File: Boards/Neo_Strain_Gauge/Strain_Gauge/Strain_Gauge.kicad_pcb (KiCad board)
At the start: 2 copper layers, 85 x 56 mm, 71 parts, among them J1 Screw_Terminal_01x03, J2 Screw_Terminal_01x03, J3 Screw_Terminal_01x03, J4 Screw_Terminal_01x03, J5 Conn_01x02, J6 USB_B_Micro, J7 Conn_02x10_Counter_Clockwise, J8 Conn_02x12_Counter_Clockwise, U1 W25Q128JVS, U2 NCP1117-3.3_SOT223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

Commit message: Hopefully final revision
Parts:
- moved TP1 0.39 mm to (147.4, 76.0)
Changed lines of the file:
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@@
   )
   (footprint "TestPoint:TestPoint_THTPad_D1.0mm_Drill0.5mm" (layer "F.Cu")
-    (at 147.61 76.36)
+    (at 147.4 76.03)
     (descr "THT pad as test Point, diameter 1.0mm, hole diameter 0.5mm")
     (tags "test point THT pad")
@@
   (segment (start 155.03103 70.64897) (end 163.51897 70.64897) (width 0.127) (layer "B.Cu") (net 77))
   (segment (start 155.08 72.27) (end 155.08 71.866886) (width 0.127) (layer "F.Cu") (net 80))
-  (segment (start 147.61 77.48) (end 147.61 76.36) (width 0.127) (layer "F.Cu") (net 80))
-  (segment (start 146.1535 78.9365) (end 147.61 77.48) (width 0.127) (layer "F.Cu") (net 80))
+  (segment (start 147.61 77.48) (end 146.1535 78.9365) (width 0.127) (layer "F.Cu") (net 80))
   (segment (start 157.06 71.2) (end 157.5625 71.2) (width 0.127) (layer "F.Cu") (net 80))
   (segment (start 151.62 73.47) (end 146.1535 78.9365) (width 0.127) (layer "F.Cu") (net 80))
   (segment (start 155.08 71.866886) (end 155.868488 71.078398) (width 0.127) (layer "F.Cu") (net 80))
   (segment (start 146.1535 78.9365) (end 134.577466 78.9365) (width 0.127) (layer "F.Cu") (net 80))
+  (segment (start 147.4 76.03) (end 147.61 76.24) (width 0.127) (layer "F.Cu") (net 80))
   (segment (start 156.938398 71.078398) (end 157.06 71.2) (width 0.127) (layer "F.Cu") (net 80))
   (segment (start 155.868488 71.078398) (end 156.938398 71.078398) (width 0.127) (layer "F.Cu") (net 80))
   (segment (start 134.577466 78.9365) (end 133.35 80.163966) (width 0.127) (layer "F.Cu") (net 80))
+  (segment (start 147.61 76.24) (end 147.61 77.48) (width 0.127) (layer "F.Cu") (net 80))
   (segment (start 133.35 80.163966) (end 133.35 80.5625) (width 0.127) (layer "F.Cu") (net 80))
   (via (at 155.08 72.27) (size 0.6) (drill 0.3) (layers "F.Cu" "B.Cu") (net 80))
@@
   (segment (start 151.62 73.47) (end 152.92 72.17) (width 0.127) (layer "B.Cu") (net 80))
   (segment (start 137.27 84.86) (end 136.16 83.75) (width 0.127) (layer "F.Cu") (net 81))
+  (segment (start 142.650412 85.514412) (end 145.795588 85.514412) (width 0.127) (layer "F.Cu") (net 81))
   (segment (start 136.16 83.75) (end 135.0375 83.75) (width 0.127) (layer "F.Cu") (net 81))
-  (segment (start 144.334824 83.83) (end 147.49 83.83) (width 0.127) (layer "F.Cu") (net 81))
   (segment (start 156.101898 71.641898) (end 156.143796 71.6) (width 0.127) (layer "F.Cu") (net 81))
-  (segment (start 142.650412 85.514412) (end 144.334824 83.83) (width 0.127) (layer "F.Cu") (net 81))
+  (segment (start 147.48 83.83) (end 147.49 83.83) (width 0.127) (layer "F.Cu") (net 81))
+  (segment (start 145.795588 85.514412) (end 147.48 83.83) (width 0.127) (layer "F.Cu") (net 81))
   (segment (start 156.143796 71.6) (end 157.5625 71.6) (width 0.127) (layer "F.Cu") (net 81))
   (via (at 142.650412 85.514412) (size 0.8) (drill 0.4) (layers "F.Cu" "B.Cu") (net 81))
   (via (at 156.101898 71.641898) (size 0.6) (drill 0.3) (layers "F.Cu" "B.Cu") (net 81))
   (via (at 137.27 84.86) (size 0.6) (drill 0.3) (layers "F.Cu" "B.Cu") (net 81))
-  (segment (start 143.39 85.09) (end 142.965588 85.514412) (width 0.127) (layer "B.Cu") (net 81))
+  (segment (start 143.39 85.09) (end 143.074824 85.09) (width 0.127) (layer "B.Cu") (net 81))
   (segment (start 152.740789 73.611659) (end 150.755948 75.5965) (width 0.127) (layer "B.Cu") (net 81))
   (segment (start 156.101898 71.641898) (end 155.8265 71.917296) (width 0.127) (layer "B.Cu") (net 81))
+  (segment (start 143.074824 85.09) (end 142.650412 85.514412) (width 0.127) (layer "B.Cu") (net 81))
   (segment (start 155.8265 71.917296) (end 155.8265 73.282069) (width 0.127) (layer "B.Cu") (net 81))
   (segment (start 155.49691 73.611659) (end 152.740789 73.611659) (width 0.127) (layer "B.Cu") (net 81))
   (segment (start 145.293 83.187) (end 143.39 85.09) (width 0.127) (layer "B.Cu") (net 81))
   (segment (start 155.8265 73.282069) (end 155.49691 73.611659) (width 0.127) (layer "B.Cu") (net 81))
-  (segment (start 142.965588 85.514412) (end 142.650412 85.514412) (width 0.127) (layer "B.Cu") (net 81))
   (segment (start 145.293 80.464552) (end 145.293 83.187) (width 0.127) (layer "B.Cu") (net 81))
   (segment (start 150.755948 75.5965) (end 150.161052 75.5965) (width 0.127) (layer "B.Cu") (net 81))

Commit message: More micro-changes without finishing the BOM
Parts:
- moved U2 2.13 mm to (158.7, 103.7)
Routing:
- net +3V3: track 192.3 -> 193.9 mm, vias 6 -> 4
- net /GPIO24: track 42.8 -> 41.9 mm
- net /REG_POWER: track 60.3 -> 61.1 mm, vias 2 -> 4

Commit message: Near finished with BOM selection
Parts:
- C17: footprint Capacitor_SMD:C_0603_1608Metric -> Capacitor_Tantalum_SMD:CP_EIA-3216-18_Kemet-A
- C19, C24, C27, C28, C29: value 0.1pF -> 100n; footprint Capacitor_SMD:C_0603_1608Metric -> Capacitor_SMD:C_0402_1005Metric
- U5: value TXB0104RGY -> TXS0104ERGYR
- moved C29 0.42 mm to (131.2, 73.3)
- moved C17 0.37 mm to (133.8, 88.2)
- moved C24 0.30 mm to (111.1, 90.5)
- moved C19 0.29 mm to (132.6, 76.8)
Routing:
- net GND: track 114.7 -> 117.9 mm
- net /GPIO23: track 47.4 -> 45.5 mm

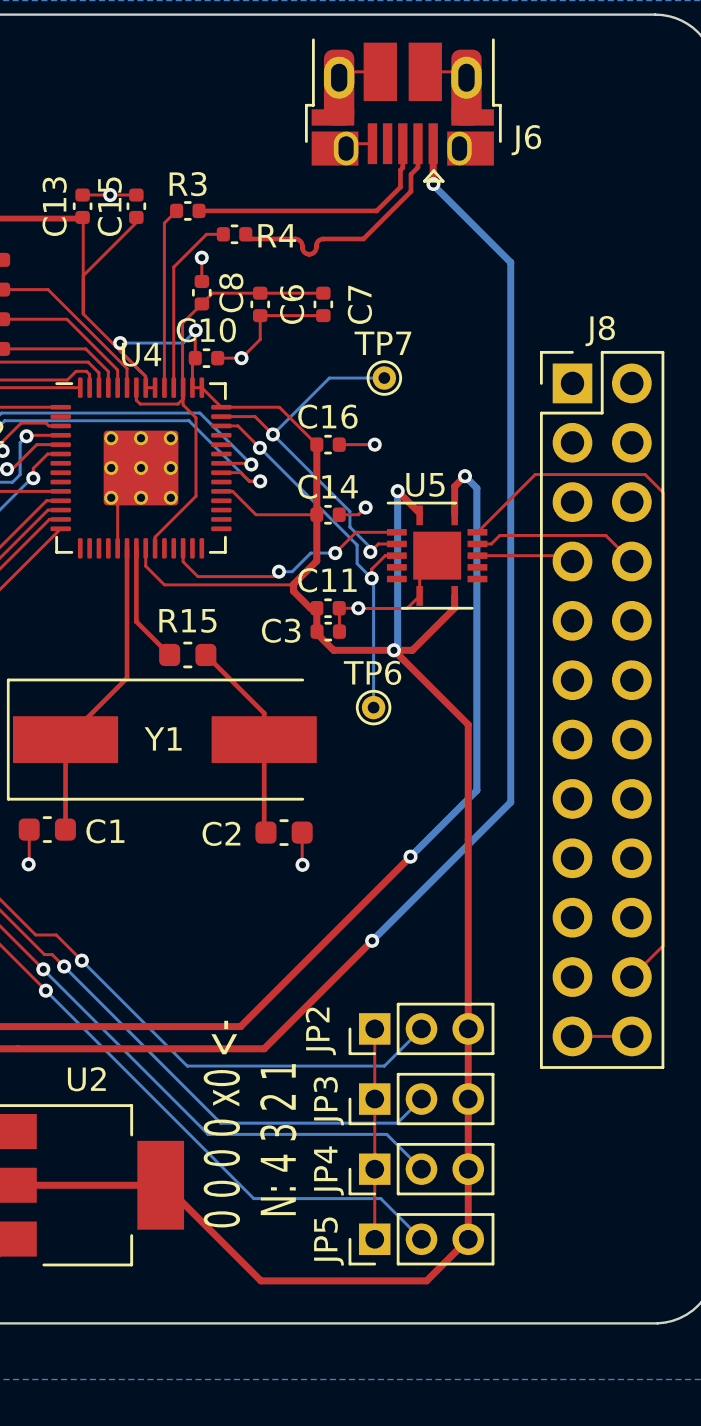
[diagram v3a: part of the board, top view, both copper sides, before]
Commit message: Finish basic BOM and update desc. in pcb
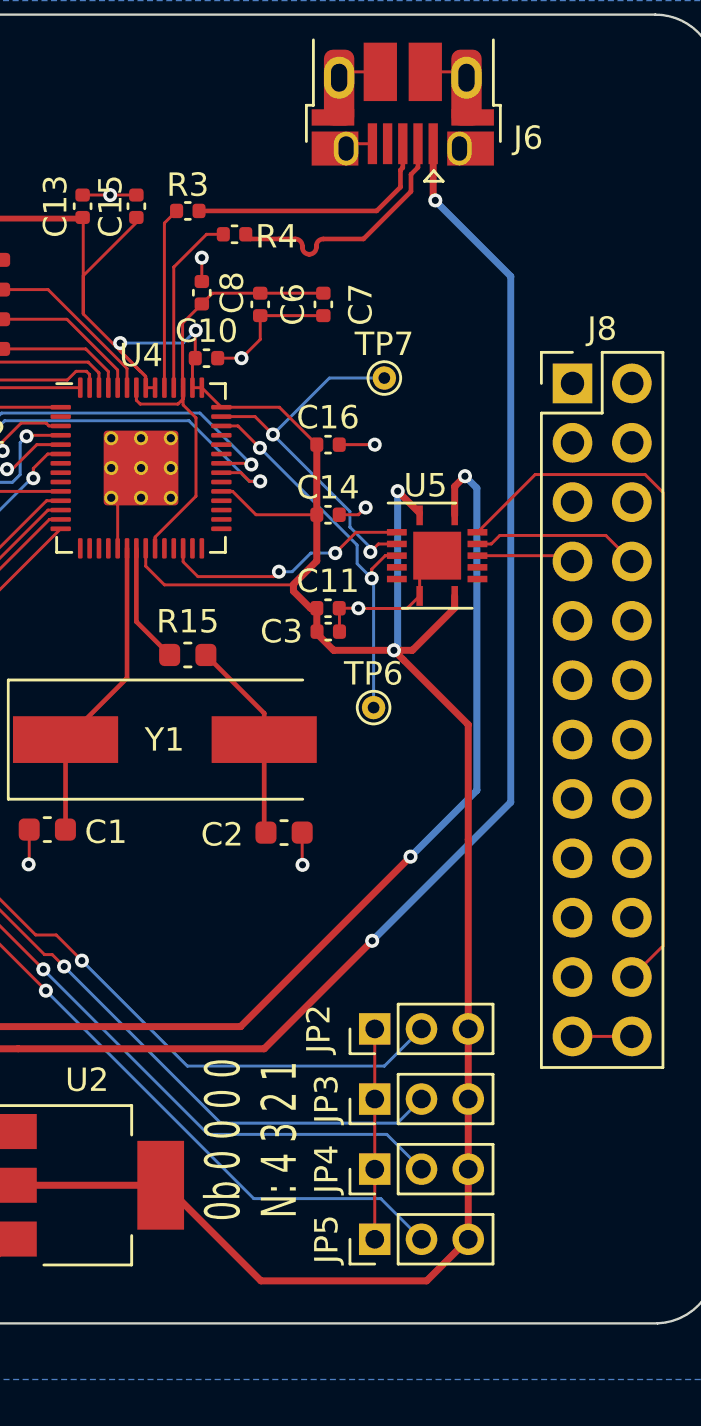
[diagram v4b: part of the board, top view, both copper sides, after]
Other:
- board text added: "0b 0 0 0 0 N: 4 3 2 1"
- board text removed: "0 0 0 0 x0 <- N: 4 3 2 1"
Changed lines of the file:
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@@
     (effects (font (size 1.5 1) (thickness 0.25)))
   )
-  (gr_text "   0 0 0 0 x0 <-\nN: 4 3 2 1" (at 165.72 101.74 90) (layer "F.SilkS")
+  (gr_text "0b 0 0 0 0\nN: 4 3 2 1" (at 165.72 101.74 90) (layer "F.SilkS")
     (effects (font (size 1.5 1) (thickness 0.125)))
   )
@@
   (segment (start 175.37 86.79) (end 172.53 89.63) (width 0.3) (layer "B.Cu") (net 100))
   (segment (start 155.74 97.85) (end 166.27 97.85) (width 0.3) (layer "F.Cu") (net 101))
-  (segment (start 173.5 60.84) (end 173.5 59.125) (width 0.3) (layer "F.Cu") (net 101))
-  (segment (start 173.51 60.85) (end 173.5 60.84) (width 0.3) (layer "F.Cu") (net 101))
   (segment (start 153.9375 97.85) (end 155.74 97.85) (width 0.3) (layer "F.Cu") (net 101))
   (segment (start 166.27 97.85) (end 170.89 93.23) (width 0.3) (layer "F.Cu") (net 101))
-  (via (at 173.51 60.85) (size 0.6) (drill 0.3) (layers "F.Cu" "B.Cu") (net 101))
+  (segment (start 173.59 61.55) (end 173.5 61.46) (width 0.3) (layer "F.Cu") (net 101))
+  (segment (start 173.5 61.46) (end 173.5 59.125) (width 0.3) (layer "F.Cu") (net 101))
+  (via (at 173.59 61.55) (size 0.6) (drill 0.3) (layers "F.Cu" "B.Cu") (net 101))
   (via (at 170.89 93.23) (size 0.6) (drill 0.3) (layers "F.Cu" "B.Cu") (net 101))
-  (segment (start 176.82 64.21) (end 176.82 87.3) (width 0.3) (layer "B.Cu") (net 101))
   (segment (start 176.82 87.3) (end 170.89 93.23) (width 0.3) (layer "B.Cu") (net 101))
-  (segment (start 173.51 60.9) (end 176.82 64.21) (width 0.3) (layer "B.Cu") (net 101))
-  (segment (start 173.51 60.85) (end 173.51 60.9) (width 0.3) (layer "B.Cu") (net 101))
+  (segment (start 173.59 61.55) (end 173.59 61.57) (width 0.3) (layer "B.Cu") (net 101))
+  (segment (start 173.59 61.57) (end 176.82 64.8) (width 0.3) (layer "B.Cu") (net 101))
+  (segment (start 176.82 64.8) (end 176.82 87.3) (width 0.3) (layer "B.Cu") (net 101))
   (zone (net 2) (net_name "GND") (layer "B.Cu") (hatch edge 0.508)
     (connect_pads (clearance 0.508))

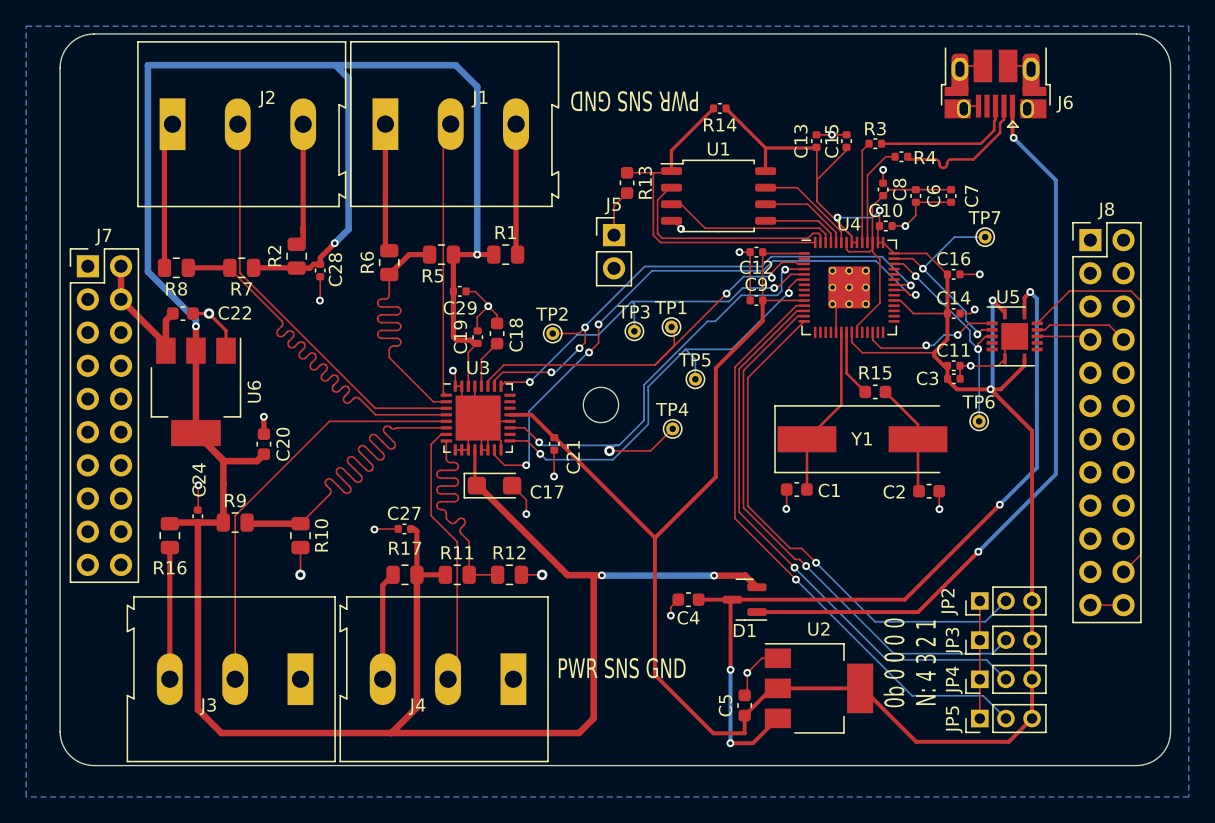
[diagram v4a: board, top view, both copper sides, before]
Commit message: Better BOM and more accurate to final design schematic, little will change from this.
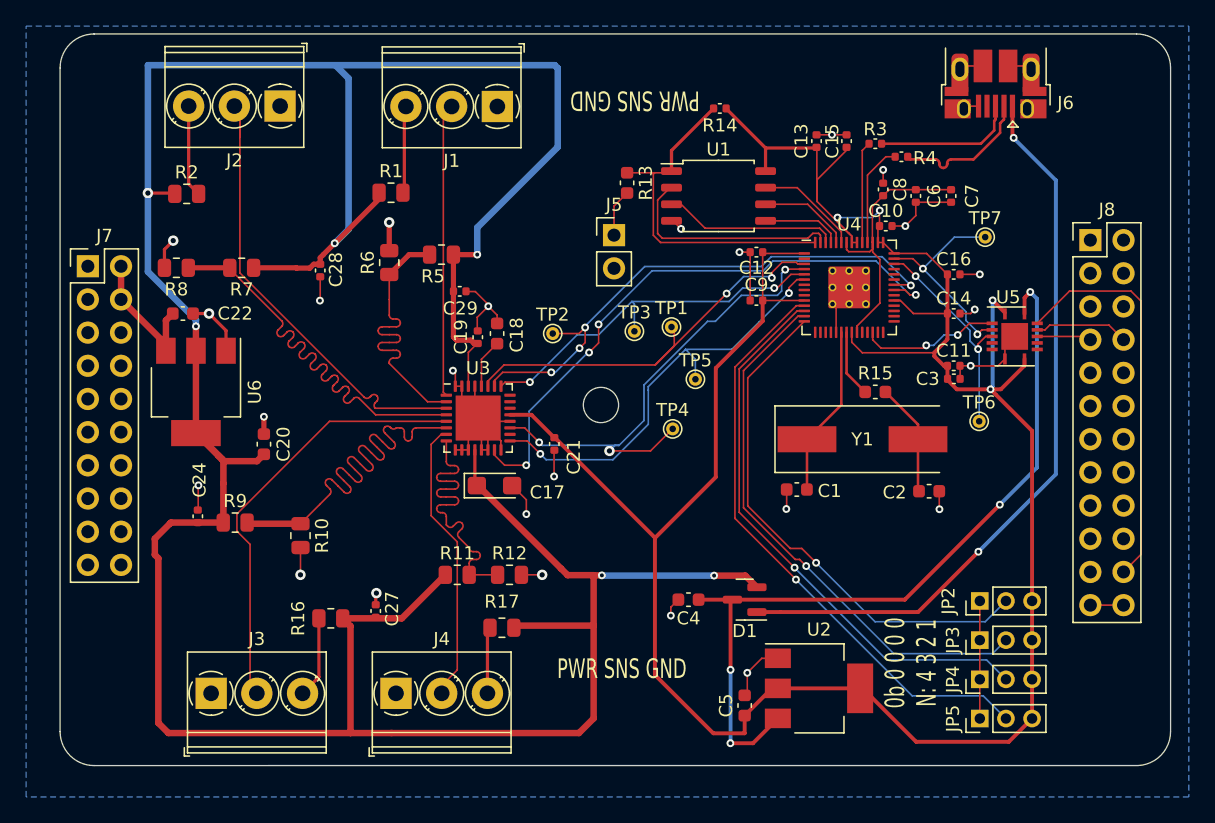
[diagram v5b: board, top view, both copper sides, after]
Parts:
- J1, J2, J3, J4: footprint TerminalBlock:TerminalBlock_Altech_AK300-3_P5.00mm -> TerminalBlock_Phoenix:TerminalBlock_Phoenix_PT-1,5-3-3.5-H_1x03_P3.50mm_Horizontal
- moved R16 13.9 mm to (121.3, 98.3), turned to 180 degrees
- moved R1 9.98 mm to (125.9, 65.8)
- moved R2 9.68 mm to (110.3, 65.8), turned to 0 degrees
- moved J4 9.05 mm to (126.3, 104.1), turned to 0 degrees
- moved J1 8.68 mm to (134.1, 59.1), turned to 180 degrees
- moved R17 8.45 mm to (134.4, 99.0)
- moved J2 8.35 mm to (117.4, 59.1), turned to 180 degrees
- moved J3 6.92 mm to (112.2, 104.1), turned to 0 degrees
- moved C27 6.65 mm to (124.8, 97.8), turned to -90 degrees
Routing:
- net +5V: track 227.9 -> 253.4 mm, vias 5 -> 6
- net GND: track 117.9 -> 100.8 mm, vias 23 -> 25
- net /IN2-: track 31.5 -> 37.2 mm
- net Net-(J3-Pad3): track 10.1 -> 6.26 mm
- net Net-(J1-Pad3): track 10.0 -> 6.69 mm
- net Net-(J4-Pad3): track 8.32 -> 5.10 mm
- net Net-(J2-Pad3): track 9.80 -> 7.04 mm
- net /IN1-: track 31.7 -> 33.7 mm
- net /IN3+: track 24.5 -> 22.9 mm
- net /IN1+: track 35.5 -> 36.9 mm
- net /IN3-: track 21.1 -> 22.5 mm
- net /IN0+: track 22.4 -> 23.7 mm
- net /IN0-: track 20.6 -> 21.9 mm

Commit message: Switch to standard pin header widths.
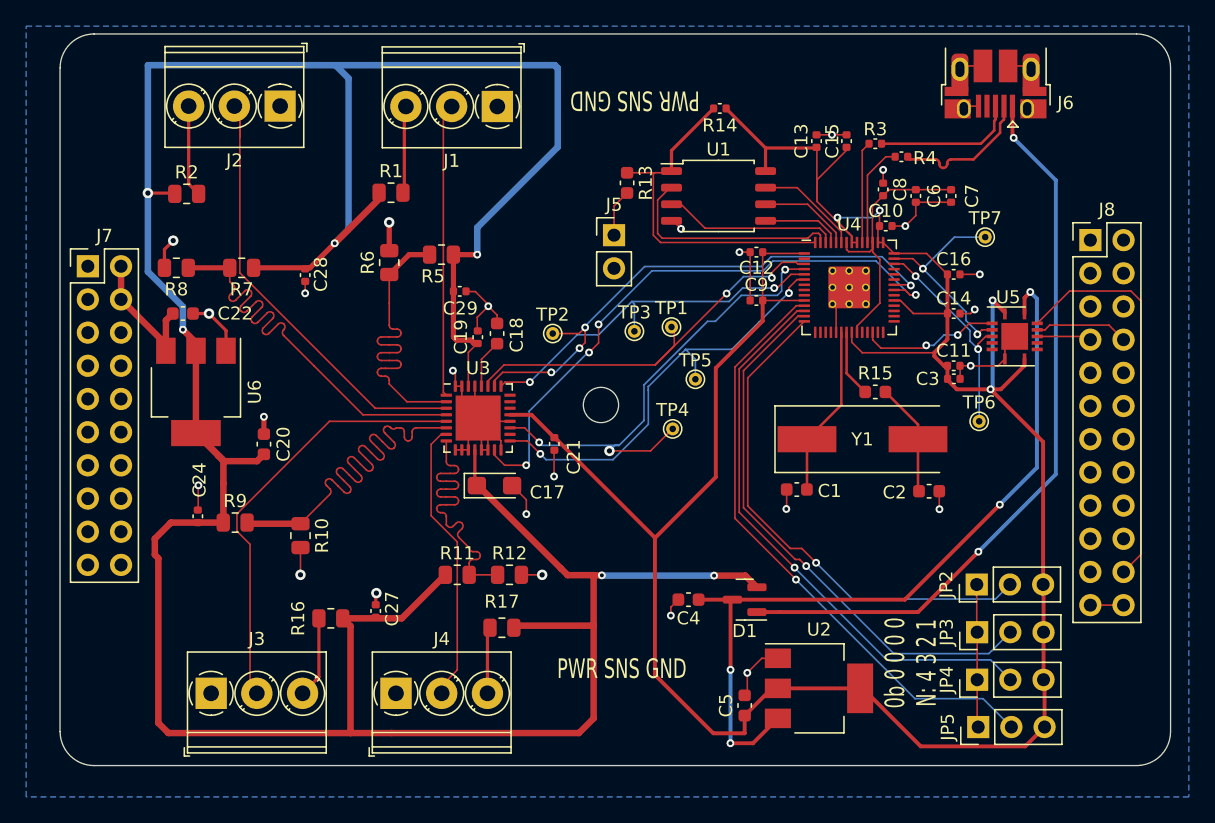
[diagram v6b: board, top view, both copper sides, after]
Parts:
- JP2, JP3, JP4, JP5: footprint Connector_PinHeader_2.00mm:PinHeader_1x03_P2.00mm_Vertical -> Connector_PinHeader_2.54mm:PinHeader_1x03_P2.54mm_Vertical
- moved JP2 1.28 mm to (170.8, 95.7)
- moved C28 1.20 mm to (119.4, 72.1)
- moved JP5 0.66 mm to (170.9, 106.7)
- moved JP3 0.64 mm to (170.8, 99.4)
- moved JP4 0.21 mm to (170.8, 103.0)
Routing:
- net /IN3+: track 22.9 -> 25.9 mm
- net +3V3: track 193.9 -> 195.9 mm
- net GND: track 100.8 -> 102.1 mm
- net /IN2+: track 34.3 -> 35.4 mm
- net /IN2-: track 37.2 -> 38.2 mm
- net /GPIO8: track 45.9 -> 46.6 mm
- net /GPIO11: track 40.0 -> 39.4 mm
- net /GPIO10: track 42.0 -> 42.6 mm
